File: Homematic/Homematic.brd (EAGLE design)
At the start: 99.2 x 85 mm, 25 parts, among them IC1 3.3V, IC2 3.3V, P1 DF11-06-2DS

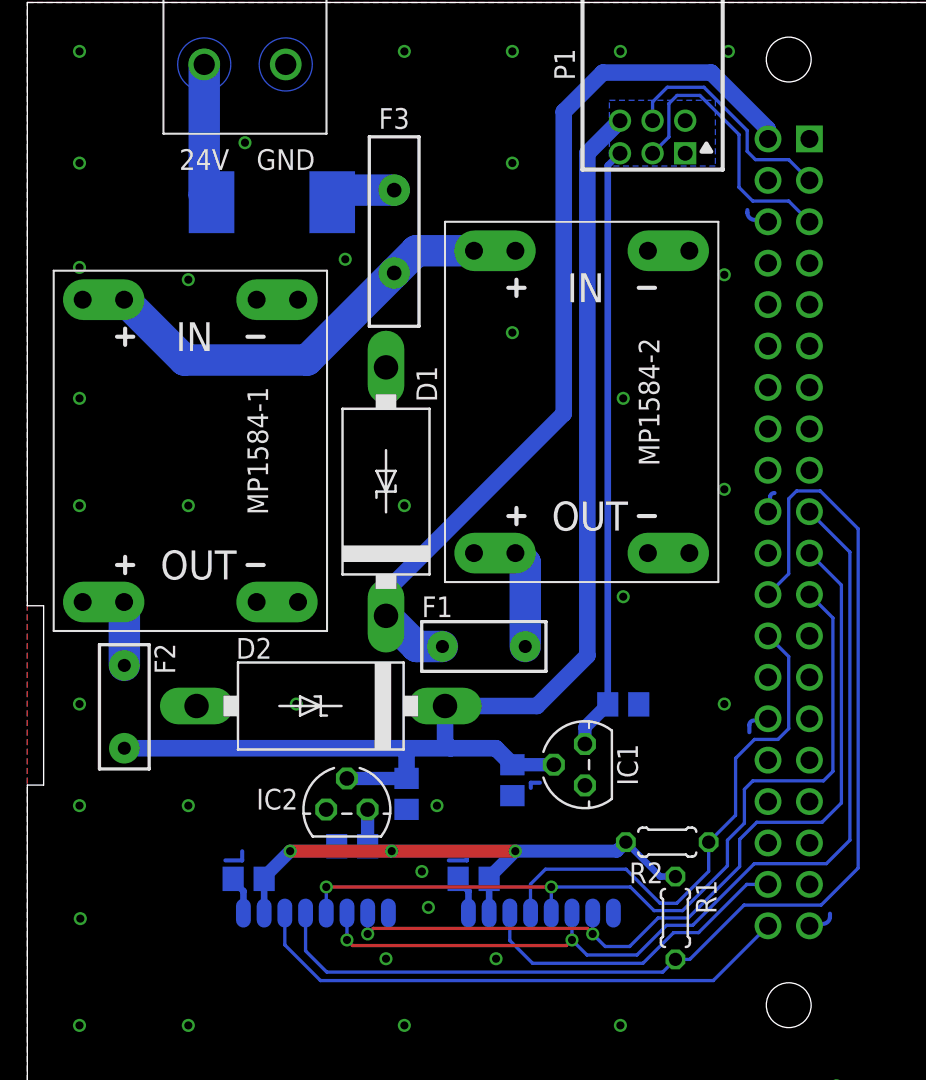
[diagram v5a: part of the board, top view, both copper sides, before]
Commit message: Fix footprint. Replace PTC.
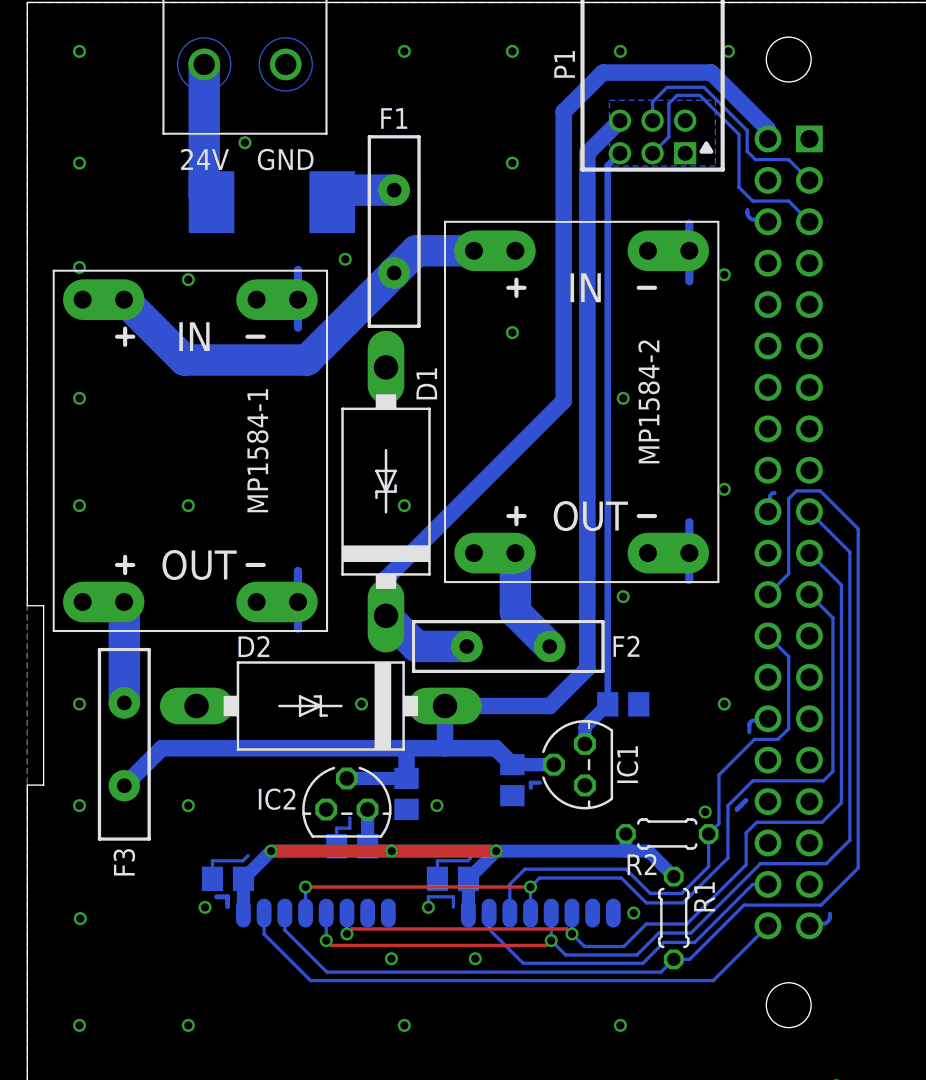
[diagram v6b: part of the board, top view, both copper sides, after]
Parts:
- F1: value 2A -> 3A; device SparkFun-Fuses:PTH -> SparkFun-Fuses:PTH_11MM
- F2: value 2A -> 2.5A; device SparkFun-Fuses:PTH -> SparkFun-Fuses:PTH_11MM
- F3: value 3A -> 2.5A
- moved F3 35.5 mm to (5.95, 38.0), turned to 270 degrees
- moved F1 26.0 mm to (22.5, 69.5), turned to 90 degrees
- moved F2 23.8 mm to (29.5, 44.0), turned to 0 degrees
- moved C1 1.27 mm to (12.3, 29.8)
- moved C6 1.27 mm to (26.1, 29.8)
- moved R2 0.50 mm to (39.2, 32.5)
- moved R1 0.10 mm to (39.6, 27.4)
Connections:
- net +5V: now also F3.P$2; no longer F2.P$2
- net N$4: now also F2.P$2; no longer F1.P$2
- net N$5: now also F2.P$1; no longer F1.P$1
- net N$6: now also F3.P$1; no longer F2.P$1
- net N$7: now also F1.P$1; no longer F3.P$1
- net N$9: now also F1.P$2; no longer F3.P$2
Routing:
- net GND: track 14.1 -> 35.9 mm, vias 96 -> 98
- net N$6: track 3.89 -> 6.19 mm
- net +3V3: track 37.5 -> 39.3 mm
- net N$5: track 55.2 -> 56.7 mm
- net N$18: track 58.9 -> 60.2 mm
- net N$17: track 53.2 -> 54.4 mm
- net +5V: track 78.7 -> 79.9 mm
- net N$16: track 52.0 -> 53.1 mm
- net N$10: track 33.9 -> 34.8 mm
- net N$19: track 20.1 -> 21.0 mm
- net N$4: track 5.98 -> 6.60 mm
- net N$15: track 32.6 -> 33.2 mm
- net N$3: track 72.0 -> 72.5 mm
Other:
- board text added: "Automation board. Version 1.3"
- board text removed: "Automation board. Version 1.2"

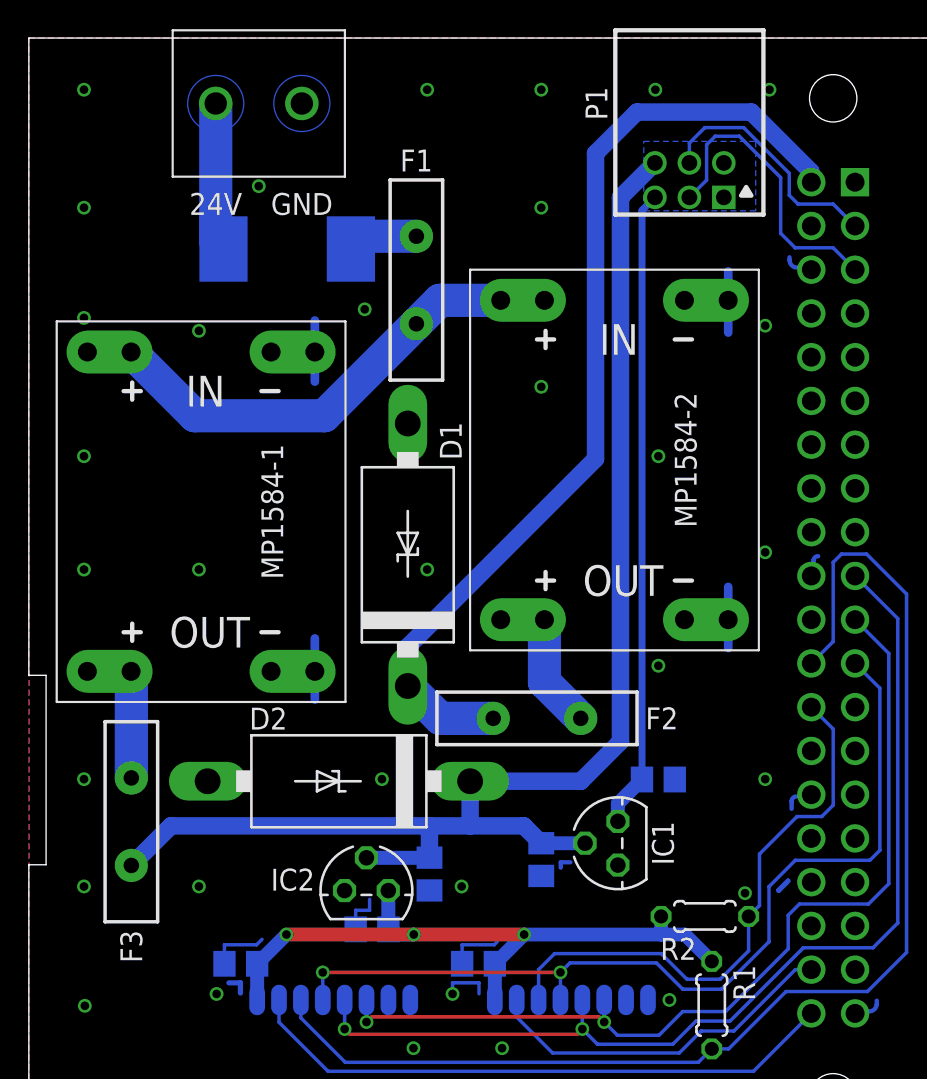
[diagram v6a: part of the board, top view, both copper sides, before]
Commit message: Add fan circuit
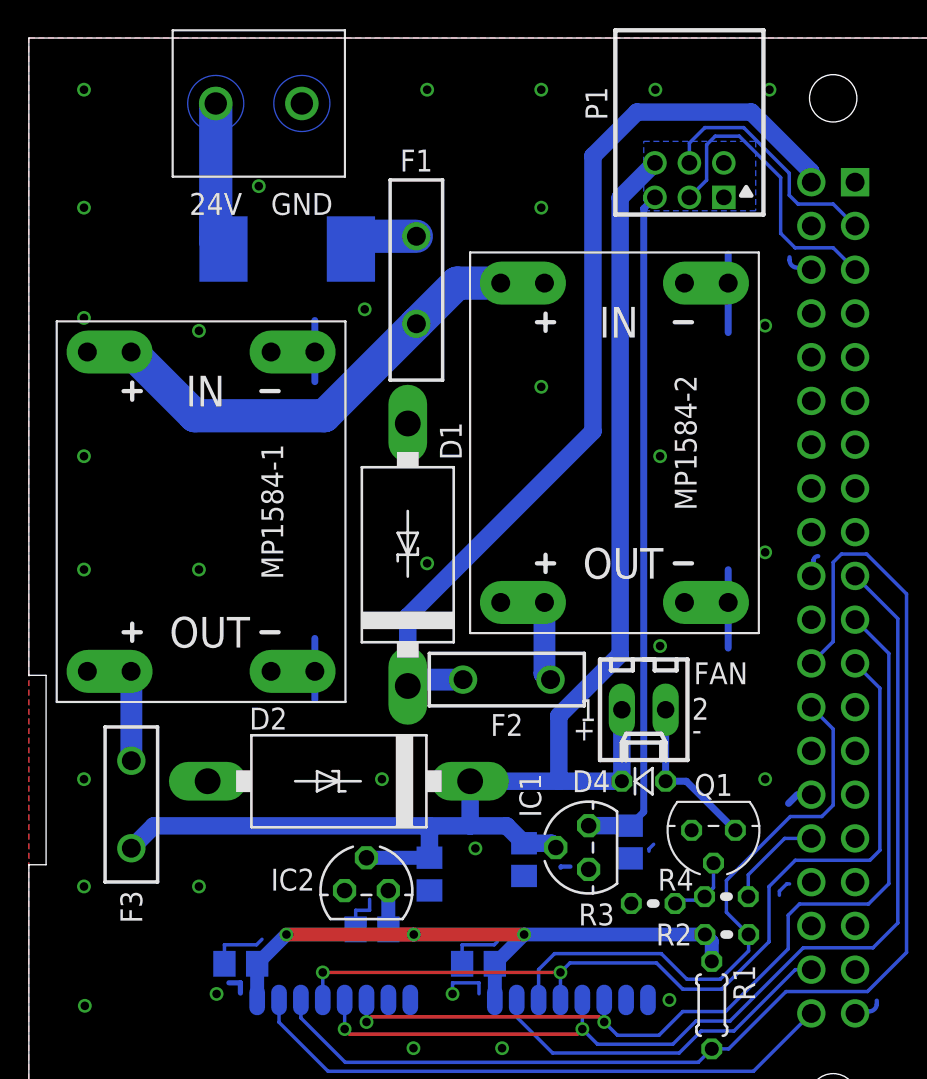
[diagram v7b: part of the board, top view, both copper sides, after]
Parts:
- added D4: 1N4148DO35-2V, diode:DO35-2V
- added FAN: 22-27-2021-02, con-molex:6410-02
- added Q1: BC337-40, transistor-npn:TO92
- added R3: 10K, rcl:0204V
- added R4: 1K8, rcl:0204V
- F1: device SparkFun-Fuses:PTH_11MM -> ptc:PTH_11MM
- F2, F3: value 2.5A -> 16V/2.5A; device SparkFun-Fuses:PTH_11MM -> ptc:RGEF250
- R2: device rcl:0204/5 -> rcl:0204V
- moved C3 3.99 mm to (34.9, 36.8), turned to 270 degrees
- moved F2 2.85 mm to (27.8, 46.2)
- moved IC1 1.72 mm to (32.5, 36.5)
- moved R2 1.65 mm to (40.5, 31.4)
- moved C2 1.00 mm to (28.8, 35.8)
- moved F3 1.00 mm to (5.95, 39.0)
- moved MP1584-2 1.00 mm to (34.0, 60.0)
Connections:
- new net N$11: Q1.2, R3.2, R4.2
- new net N$13: R4.1, RPI.32
- new net N$14: D4.A, FAN.2, Q1.3
- net +5V: now also D4.C, FAN.1
- net GND: now also Q1.1, R3.1
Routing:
- net N$14: track 0.00 -> 9.38 mm
- net N$13: track 0.00 -> 5.80 mm
- net +5V: track 79.9 -> 85.0 mm
- net N$11: track 0.00 -> 4.04 mm
- net N$5: track 56.7 -> 54.4 mm
- net N$2: track 37.1 -> 39.5 mm
- net N$4: track 6.60 -> 4.63 mm
- net GND: track 35.9 -> 37.4 mm, vias 98 -> 97
- net N$15: track 33.2 -> 34.5 mm
- net N$6: track 6.19 -> 5.19 mm
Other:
- board text added: "+"
- board text added: "-"

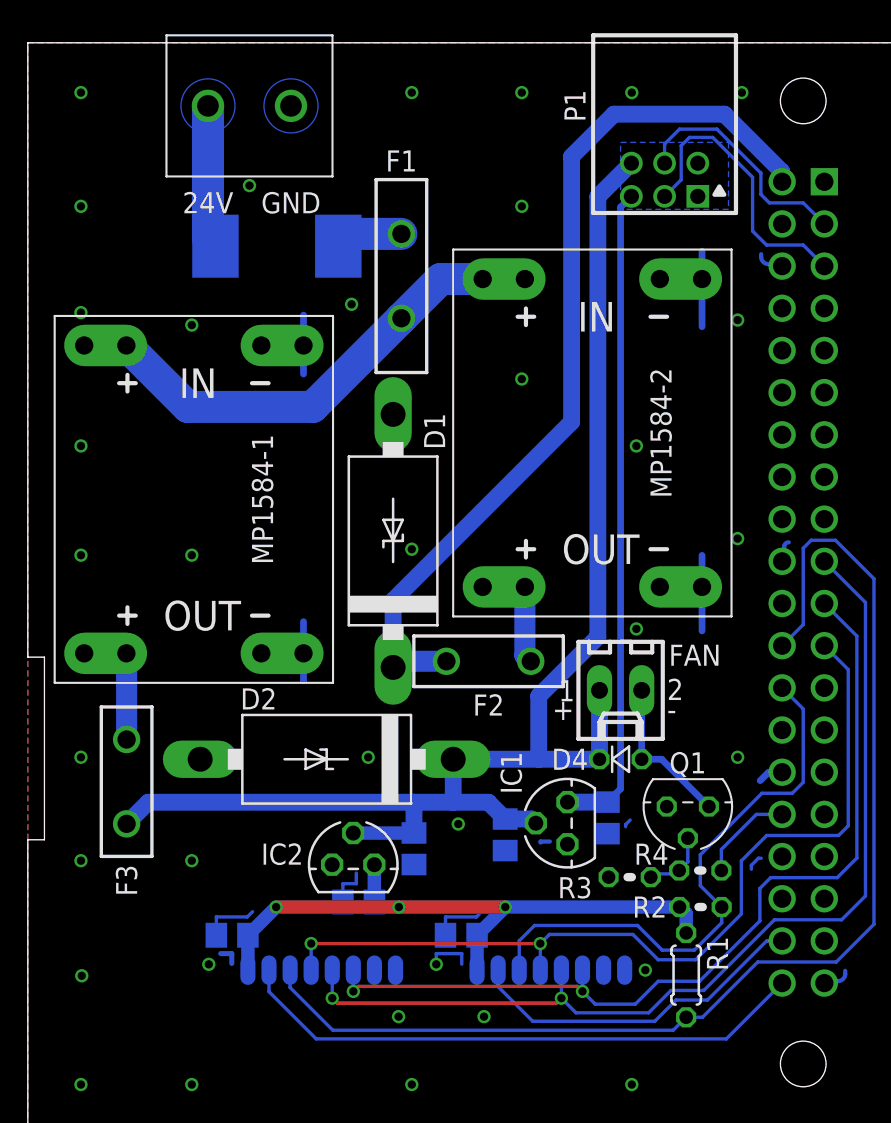
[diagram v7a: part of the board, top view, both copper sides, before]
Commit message: Use SMD PTC's instead of through hole ones.
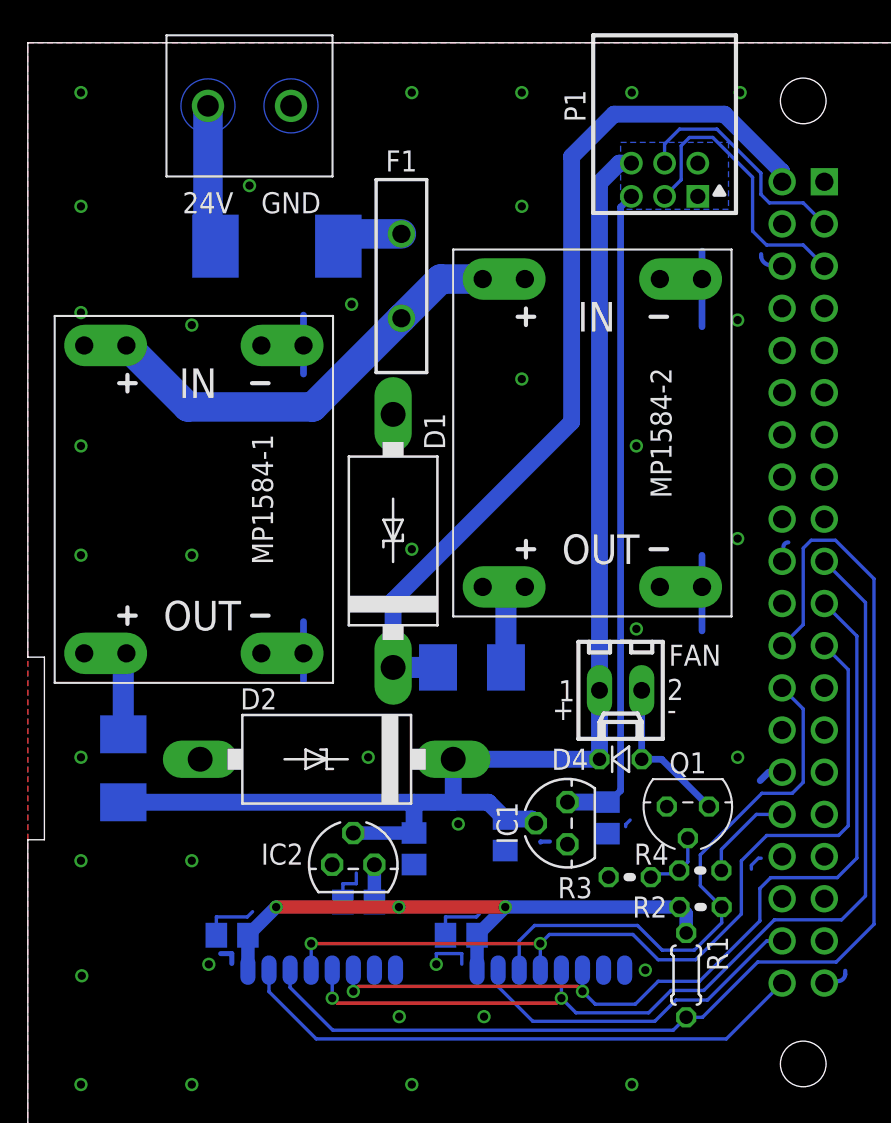
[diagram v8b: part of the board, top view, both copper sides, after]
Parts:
- F2, F3: value 16V/2.5A -> 5V/2.5A; device ptc:RGEF250 -> adafruit:1812
- moved F2 1.07 mm to (26.8, 45.9), flipped to the bottom, turned to 180 degrees
- moved F3 0.83 mm to (5.75, 39.8), flipped to the bottom
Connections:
- net +5V: now also F3.2; no longer F3.P$2
- net N$4: now also F2.2; no longer F2.P$2
- net N$5: now also F2.1; no longer F2.P$1
- net N$6: now also F3.1; no longer F3.P$1
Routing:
- net +5V: track 85.0 -> 79.4 mm
- net N$4: track 4.63 -> 5.99 mm
- net N$5: track 54.4 -> 53.7 mm
